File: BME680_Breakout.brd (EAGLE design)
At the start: 160 x 100 mm, 14 parts, among them U1 BME680, U4 PCA9515ADP

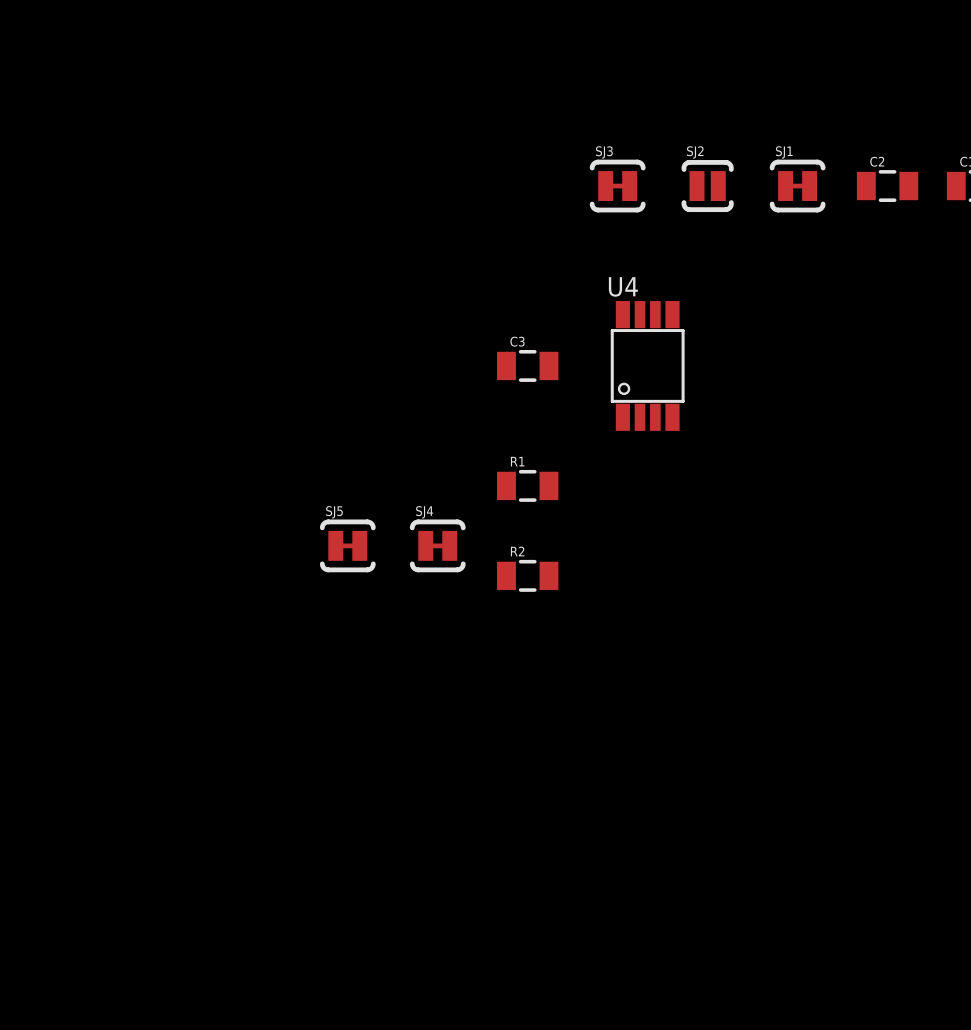
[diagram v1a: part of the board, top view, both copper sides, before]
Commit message: added some support for SPI and wired an 8-pin interface header
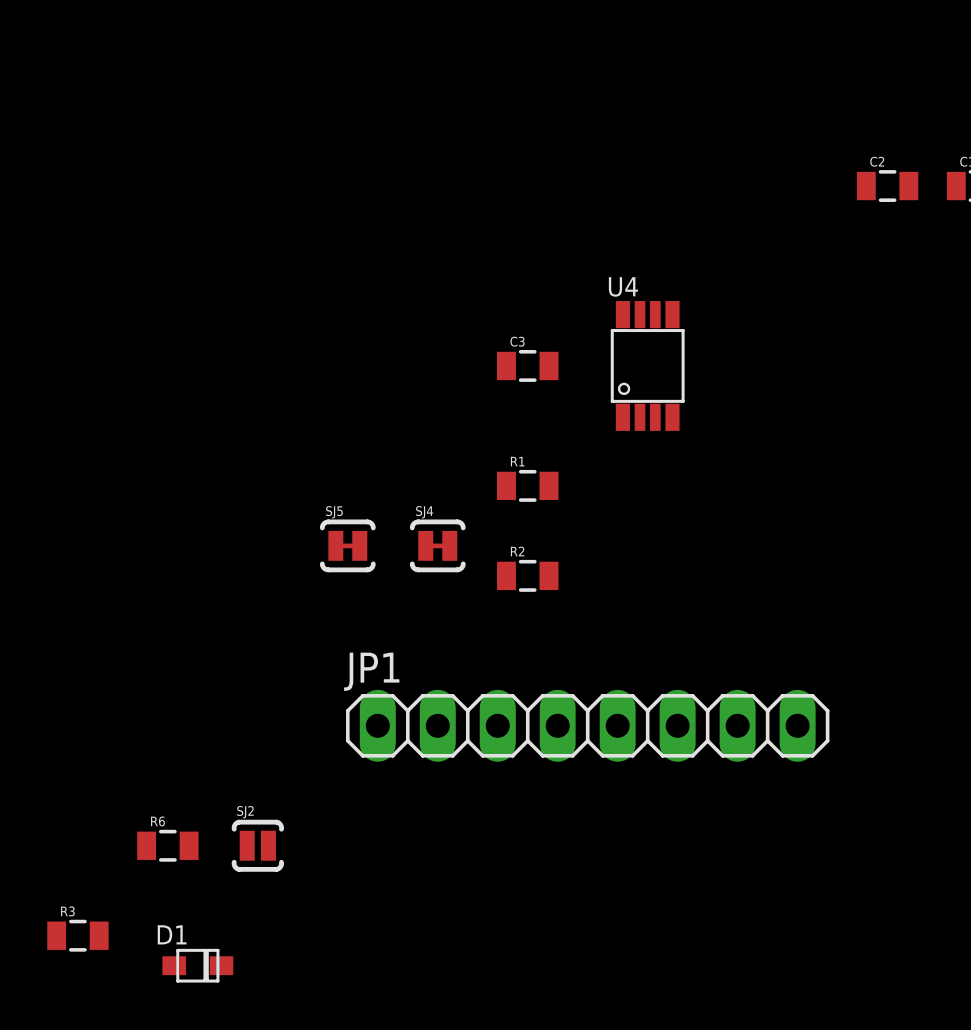
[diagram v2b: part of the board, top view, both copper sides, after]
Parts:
- removed SJ1, SJ3: JUMPER-PAD-2-NC_BY_TRACE, SparkFun-Passives:PAD-JUMPER-2-NC_BY_TRACE_YES_SILK
- added D1: (no value), adafruit:SOD-323F
- added JP1: (no value), pinhead:1X08
- added R3, R6: 10k, SparkFun-Passives:0805
- moved SJ2 33.8 mm to (-49.5, -25.4)
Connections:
- new net CSB_VCCIO: D1.C, JP1.6
- net 3.3V: now also JP1.8, R3.1, R6.1; no longer SJ2.2, SJ3.2
- net ADDR_SELECT_3V3: now also JP1.7, R3.2, SJ2.2; no longer SJ1.2, SJ2.1
- net CSB_3V3: now also D1.A, R6.2; no longer SJ3.1
- net GND: now also JP1.2, SJ2.1; no longer SJ1.1
- net MASTER_SCL_VIO: now also JP1.3
- net MASTER_SDA_VIO: now also JP1.4
- net SLAVE_I2C_ENABLE: now also JP1.5
- net VCCIO: now also JP1.1
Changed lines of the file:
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@@
 <element name="R5" library="SparkFun-Passives" package="0805" value="4.7k" x="-19.05" y="11.43"/>
 <element name="U1" library="wicked-device" package="BME680" value="BME680" x="-15.24" y="3.81"/>
-<element name="SJ1" library="SparkFun-Passives" package="PAD-JUMPER-2-NC_BY_TRACE_YES_SILK" value="JUMPER-PAD-2-NC_BY_TRACE" x="-26.67" y="2.54"/>
-<element name="SJ2" library="SparkFun-Passives" package="PAD-JUMPER-2-NO_YES_SILK" value="JUMPER-PAD-2-NOYES_SILK" x="-30.48" y="2.54"/>
-<element name="SJ3" library="SparkFun-Passives" package="PAD-JUMPER-2-NC_BY_TRACE_YES_SILK" value="JUMPER-PAD-2-NC_BY_TRACE" x="-34.29" y="2.54"/>
 <element name="U4" library="PCA9515ADP" package="SOT505-1" value="PCA9515ADP" x="-33.02" y="-5.08"/>
 <element name="C3" library="SparkFun-Passives" package="0805" value="0.1uF" x="-38.1" y="-5.08"/>
@@
 <element name="SJ4" library="SparkFun-Passives" package="PAD-JUMPER-2-NC_BY_TRACE_YES_SILK" value="JUMPER-PAD-2-NC_BY_TRACE" x="-41.91" y="-12.7"/>
 <element name="SJ5" library="SparkFun-Passives" package="PAD-JUMPER-2-NC_BY_TRACE_YES_SILK" value="JUMPER-PAD-2-NC_BY_TRACE" x="-45.72" y="-12.7"/>
+<element name="JP1" library="pinhead" package="1X08" value="" x="-35.56" y="-20.32"/>
+<element name="SJ2" library="SparkFun-Passives" package="PAD-JUMPER-2-NO_YES_SILK" value="JUMPER-PAD-2-NOYES_SILK" x="-49.53" y="-25.4"/>
+<element name="R6" library="SparkFun-Passives" package="0805" value="10k" x="-53.34" y="-25.4"/>
+<element name="D1" library="adafruit" package="SOD-323F" value="" x="-52.07" y="-30.48"/>
+<element name="R3" library="SparkFun-Passives" package="0805" value="10k" x="-57.15" y="-29.21"/>
 </elements>
 <signals>
@@
 <contactref element="R4" pad="1"/>
 <contactref element="R5" pad="1"/>
-<contactref element="SJ2" pad="2"/>
-<contactref element="SJ3" pad="2"/>
 <contactref element="U4" pad="8"/>
 <contactref element="C3" pad="1"/>
+<contactref element="R6" pad="1"/>
+<contactref element="R3" pad="1"/>
+<contactref element="JP1" pad="8"/>
+<wire x1="-54.24" y1="-25.4" x2="-58.05" y2="-29.21" width="0" layer="19" extent="1-1"/>
+<wire x1="-39" y1="-5.08" x2="-54.24" y2="-25.4" width="0" layer="19" extent="1-1"/>
 <wire x1="-34.07" y1="-2.905" x2="-39" y2="-5.08" width="0" layer="19" extent="1-1"/>
-<wire x1="-33.782" y1="2.54" x2="-34.07" y2="-2.905" width="0" layer="19" extent="1-1"/>
-<wire x1="-30.03" y1="2.54" x2="-33.782" y2="2.54" width="0" layer="19" extent="1-1"/>
-<wire x1="-23.76" y1="2.54" x2="-30.03" y2="2.54" width="0" layer="19" extent="1-1"/>
+<wire x1="-23.76" y1="2.54" x2="-34.07" y2="-2.905" width="0" layer="19" extent="1-1"/>
 <wire x1="-19.95" y1="2.54" x2="-23.76" y2="2.54" width="0" layer="19" extent="1-1"/>
 <wire x1="-16.5275" y1="3.41" x2="-19.95" y2="2.54" width="0" layer="19" extent="1-1"/>
@@
 <wire x1="-16.14" y1="11.43" x2="-16.5275" y2="5.01" width="0" layer="19" extent="1-1"/>
 <wire x1="-19.95" y1="11.43" x2="-16.14" y2="11.43" width="0" layer="19" extent="1-1"/>
+<wire x1="-26.67" y1="-20.32" x2="-34.07" y2="-2.905" width="0" layer="19" extent="1-1"/>
 </signal>
 <signal name="GND">
@@
 <contactref element="U1" pad="1"/>
 <contactref element="U1" pad="7"/>
-<contactref element="SJ1" pad="1"/>
 <contactref element="U4" pad="4"/>
 <contactref element="C3" pad="2"/>
+<contactref element="SJ2" pad="1"/>
+<contactref element="JP1" pad="2"/>
+<wire x1="-41.91" y1="-20.32" x2="-49.98" y2="-25.4" width="0" layer="19" extent="1-1"/>
+<wire x1="-37.2" y1="-5.08" x2="-41.91" y2="-20.32" width="0" layer="19" extent="1-1"/>
 <wire x1="-31.97" y1="-7.255" x2="-37.2" y2="-5.08" width="0" layer="19" extent="1-1"/>
-<wire x1="-27.178" y1="2.54" x2="-31.97" y2="-7.255" width="0" layer="19" extent="1-1"/>
-<wire x1="-21.96" y1="2.54" x2="-27.178" y2="2.54" width="0" layer="19" extent="1-1"/>
+<wire x1="-21.96" y1="2.54" x2="-31.97" y2="-7.255" width="0" layer="19" extent="1-1"/>
 <wire x1="-18.15" y1="2.54" x2="-21.96" y2="2.54" width="0" layer="19" extent="1-1"/>
 <wire x1="-16.5275" y1="4.21" x2="-18.15" y2="2.54" width="0" layer="19" extent="1-1"/>
@@
 <signal name="CSB_3V3">
 <contactref element="U1" pad="2"/>
-<contactref element="SJ3" pad="1"/>
-<wire x1="-13.9525" y1="4.21" x2="-34.798" y2="2.54" width="0" layer="19" extent="1-1"/>
+<contactref element="R6" pad="2"/>
+<contactref element="D1" pad="A"/>
+<wire x1="-52.44" y1="-25.4" x2="-53.07" y2="-30.48" width="0" layer="19" extent="1-1"/>
+<wire x1="-13.9525" y1="4.21" x2="-52.44" y2="-25.4" width="0" layer="19" extent="1-1"/>
 </signal>
 <signal name="ADDR_SELECT_3V3">
 <contactref element="U1" pad="5"/>
-<contactref element="SJ2" pad="1"/>
-<contactref element="SJ1" pad="2"/>
-<wire x1="-26.162" y1="2.54" x2="-30.93" y2="2.54" width="0" layer="19" extent="1-1"/>
-<wire x1="-16.5275" y1="2.61" x2="-26.162" y2="2.54" width="0" layer="19" extent="1-1"/>
+<contactref element="SJ2" pad="2"/>
+<contactref element="R3" pad="2"/>
+<contactref element="JP1" pad="7"/>
+<wire x1="-49.08" y1="-25.4" x2="-56.25" y2="-29.21" width="0" layer="19" extent="1-1"/>
+<wire x1="-29.21" y1="-20.32" x2="-49.08" y2="-25.4" width="0" layer="19" extent="1-1"/>
+<wire x1="-16.5275" y1="2.61" x2="-29.21" y2="-20.32" width="0" layer="19" extent="1-1"/>
 </signal>
 <signal name="SLAVE_SCL_3V3">
@@
 <signal name="MASTER_SCL_VIO">
 <contactref element="U4" pad="2"/>
+<contactref element="JP1" pad="3"/>
+<wire x1="-33.345" y1="-7.255" x2="-39.37" y2="-20.32" width="0" layer="19" extent="1-1"/>
 </signal>
 <signal name="MASTER_SDA_VIO">
 <contactref element="U4" pad="3"/>
+<contactref element="JP1" pad="4"/>
+<wire x1="-32.695" y1="-7.255" x2="-36.83" y2="-20.32" width="0" layer="19" extent="1-1"/>
 </signal>
 <signal name="SLAVE_I2C_ENABLE">
 <contactref element="U4" pad="5"/>
+<contactref element="JP1" pad="5"/>
+<wire x1="-31.97" y1="-2.905" x2="-34.29" y2="-20.32" width="0" layer="19" extent="1-1"/>
 </signal>
 <signal name="SLAVE_SDA_3V3">
@@
 <contactref element="R1" pad="1"/>
 <contactref element="R2" pad="1"/>
+<contactref element="JP1" pad="1"/>
+<wire x1="-39" y1="-13.97" x2="-44.45" y2="-20.32" width="0" layer="19" extent="1-1"/>
 <wire x1="-39" y1="-10.16" x2="-39" y2="-13.97" width="0" layer="19" extent="1-1"/>
 </signal>
@@
 <contactref element="SJ5" pad="1"/>
 </signal>
+<signal name="CSB_VCCIO">
+<contactref element="D1" pad="C"/>
+<contactref element="JP1" pad="6"/>
+<wire x1="-31.75" y1="-20.32" x2="-51.07" y2="-30.48" width="0" layer="19" extent="1-1"/>
+</signal>
 </signals>

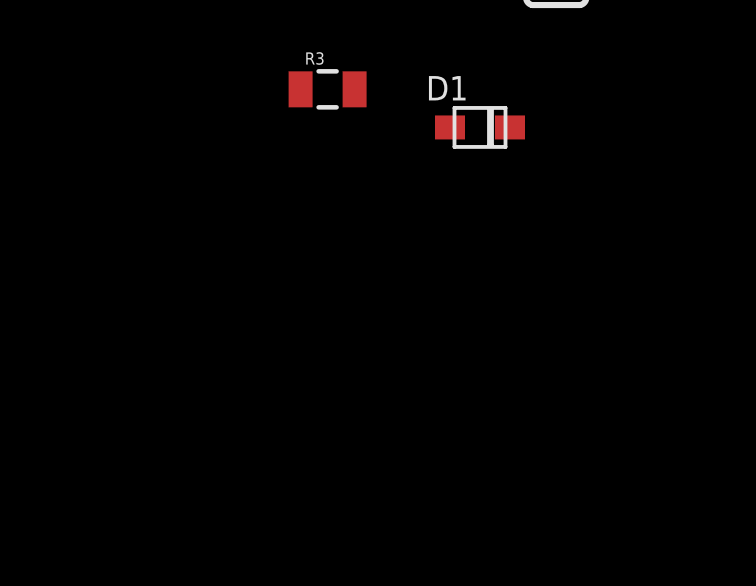
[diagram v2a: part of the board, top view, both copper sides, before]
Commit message: added input power regulator, still need bypass solution, reorganized schematic slightly
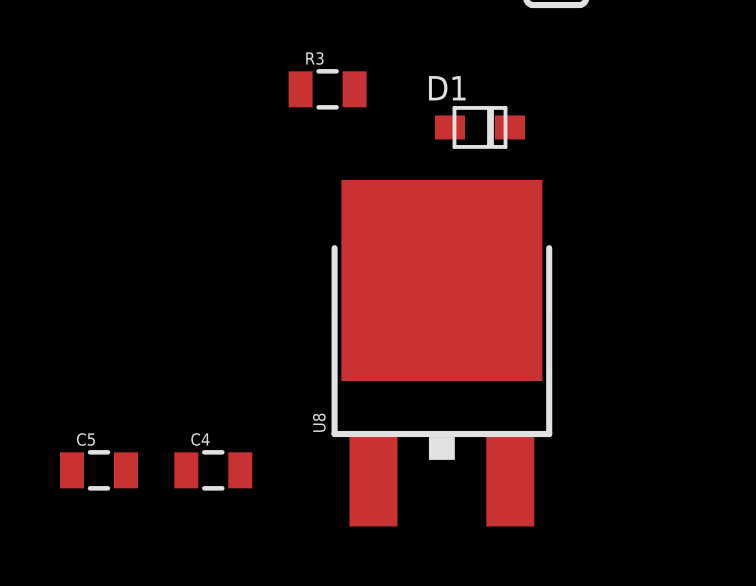
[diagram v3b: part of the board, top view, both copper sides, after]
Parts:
- added C4, C5: 10uF, SparkFun-Passives:0805
- added U8: LD1117XX, wicked-device:DPAK
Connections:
- net 3.3V: now also C5.1, U8.4
- net GND: now also C4.2, C5.2, U8.1
- net VCCIO: now also C4.1, U8.3
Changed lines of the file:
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@@
 <layer number="113" name="IDFDebug" color="4" fill="1" visible="yes" active="yes"/>
 <layer number="116" name="Patch_BOT" color="9" fill="4" visible="yes" active="yes"/>
+<layer number="118" name="Rect_Pads" color="7" fill="1" visible="no" active="yes"/>
 <layer number="121" name="_tsilk" color="7" fill="1" visible="yes" active="yes"/>
 <layer number="122" name="_bsilk" color="7" fill="1" visible="yes" active="yes"/>
@@
 <layer number="223" name="223bmp" color="24" fill="1" visible="no" active="no"/>
 <layer number="224" name="224bmp" color="25" fill="1" visible="no" active="no"/>
+<layer number="231" name="Eagle3D_PG1" color="7" fill="1" visible="yes" active="yes"/>
+<layer number="232" name="Eagle3D_PG2" color="7" fill="1" visible="yes" active="yes"/>
+<layer number="233" name="Eagle3D_PG3" color="7" fill="1" visible="yes" active="yes"/>
 <layer number="248" name="Housing" color="7" fill="1" visible="yes" active="yes"/>
 <layer number="249" name="Edge" color="7" fill="1" visible="yes" active="yes"/>
@@
 <element name="D1" library="adafruit" package="SOD-323F" value="" x="-52.07" y="-30.48"/>
 <element name="R3" library="SparkFun-Passives" package="0805" value="10k" x="-57.15" y="-29.21"/>
+<element name="U8" library="wicked-device" package="DPAK" value="LD1117XX" x="-53.34" y="-39.37"/>
+<element name="C4" library="SparkFun-Passives" package="0805" value="10uF" x="-60.96" y="-41.91"/>
+<element name="C5" library="SparkFun-Passives" package="0805" value="10uF" x="-64.77" y="-41.91"/>
 </elements>
 <signals>
@@
 <contactref element="R3" pad="1"/>
 <contactref element="JP1" pad="8"/>
+<contactref element="U8" pad="4"/>
+<contactref element="C5" pad="1"/>
+<wire x1="-53.34" y1="-35.582" x2="-65.67" y2="-41.91" width="0" layer="19" extent="1-1"/>
+<wire x1="-58.05" y1="-29.21" x2="-53.34" y2="-35.582" width="0" layer="19" extent="1-1"/>
 <wire x1="-54.24" y1="-25.4" x2="-58.05" y2="-29.21" width="0" layer="19" extent="1-1"/>
 <wire x1="-39" y1="-5.08" x2="-54.24" y2="-25.4" width="0" layer="19" extent="1-1"/>
@@
 <contactref element="SJ2" pad="1"/>
 <contactref element="JP1" pad="2"/>
+<contactref element="U8" pad="1"/>
+<contactref element="C4" pad="2"/>
+<contactref element="C5" pad="2"/>
+<wire x1="-60.06" y1="-41.91" x2="-63.87" y2="-41.91" width="0" layer="19" extent="1-1"/>
+<wire x1="-55.62" y1="-42.28" x2="-60.06" y2="-41.91" width="0" layer="19" extent="1-1"/>
+<wire x1="-49.98" y1="-25.4" x2="-55.62" y2="-42.28" width="0" layer="19" extent="1-1"/>
 <wire x1="-41.91" y1="-20.32" x2="-49.98" y2="-25.4" width="0" layer="19" extent="1-1"/>
 <wire x1="-37.2" y1="-5.08" x2="-41.91" y2="-20.32" width="0" layer="19" extent="1-1"/>
@@
 <contactref element="R2" pad="1"/>
 <contactref element="JP1" pad="1"/>
+<contactref element="U8" pad="3"/>
+<contactref element="C4" pad="1"/>
+<wire x1="-51.06" y1="-42.28" x2="-61.86" y2="-41.91" width="0" layer="19" extent="1-1"/>
+<wire x1="-44.45" y1="-20.32" x2="-51.06" y2="-42.28" width="0" layer="19" extent="1-1"/>
 <wire x1="-39" y1="-13.97" x2="-44.45" y2="-20.32" width="0" layer="19" extent="1-1"/>
 <wire x1="-39" y1="-10.16" x2="-39" y2="-13.97" width="0" layer="19" extent="1-1"/>

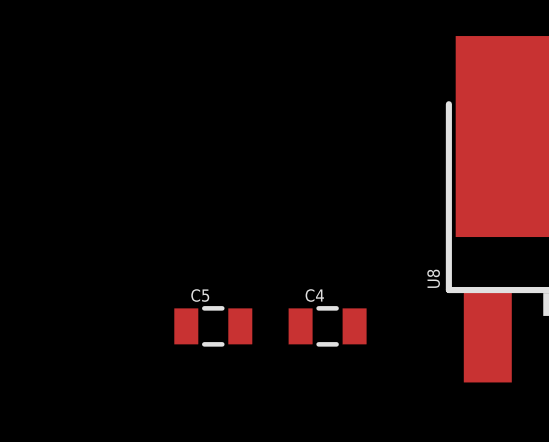
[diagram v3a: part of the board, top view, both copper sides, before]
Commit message: added pull-down hardware option to allow changing default behavior of i2c buffer
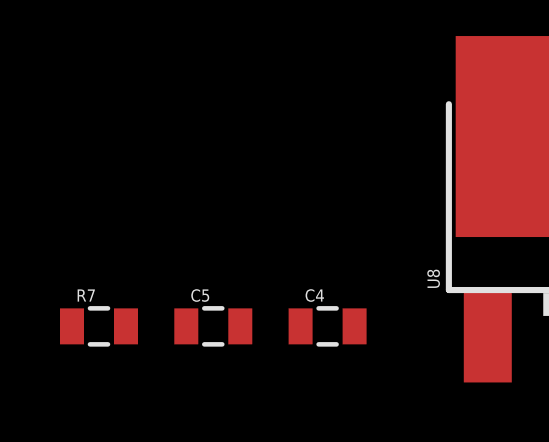
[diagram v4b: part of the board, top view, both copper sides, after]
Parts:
- added R7: 10k_DNP, SparkFun-Passives:0805
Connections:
- net CSB_VCCIO renamed CSB_VIO
- net GND: now also R7.2
- net SLAVE_I2C_ENABLE: now also R7.1
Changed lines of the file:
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@@
 <element name="C4" library="SparkFun-Passives" package="0805" value="10uF" x="-60.96" y="-41.91"/>
 <element name="C5" library="SparkFun-Passives" package="0805" value="10uF" x="-64.77" y="-41.91"/>
+<element name="R7" library="SparkFun-Passives" package="0805" value="10k_DNP" x="-68.58" y="-41.91"/>
 </elements>
 <signals>
@@
 <contactref element="C4" pad="2"/>
 <contactref element="C5" pad="2"/>
+<contactref element="R7" pad="2"/>
+<wire x1="-63.87" y1="-41.91" x2="-67.68" y2="-41.91" width="0" layer="19" extent="1-1"/>
 <wire x1="-60.06" y1="-41.91" x2="-63.87" y2="-41.91" width="0" layer="19" extent="1-1"/>
 <wire x1="-55.62" y1="-42.28" x2="-60.06" y2="-41.91" width="0" layer="19" extent="1-1"/>
@@
 <contactref element="U4" pad="5"/>
 <contactref element="JP1" pad="5"/>
+<contactref element="R7" pad="1"/>
+<wire x1="-34.29" y1="-20.32" x2="-69.48" y2="-41.91" width="0" layer="19" extent="1-1"/>
 <wire x1="-31.97" y1="-2.905" x2="-34.29" y2="-20.32" width="0" layer="19" extent="1-1"/>
 </signal>
@@
 <contactref element="SJ5" pad="1"/>
 </signal>
-<signal name="CSB_VCCIO">
+<signal name="CSB_VIO">
 <contactref element="D1" pad="C"/>
 <contactref element="JP1" pad="6"/>

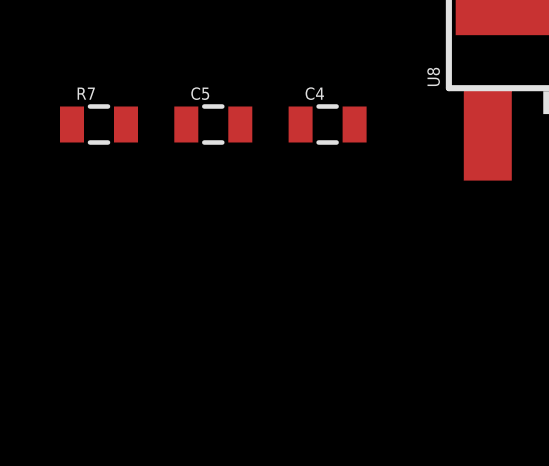
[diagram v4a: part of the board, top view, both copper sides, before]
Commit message: added a few internal test points
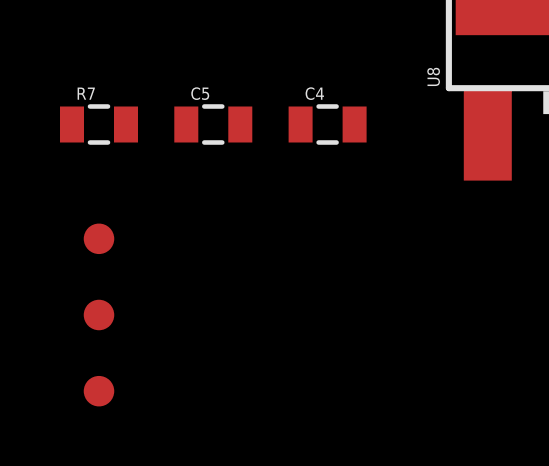
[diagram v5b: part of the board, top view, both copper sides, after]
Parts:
- added TP1, TP2, TP3: TEST-POINT3X4, SparkFun-Passives:PAD.03X.04
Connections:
- removed net N$1: R1.2, SJ4.2
- removed net N$2: R2.2, SJ5.2
- new net SJ_MASTER_SCL_3V3: R2.2, SJ5.2, TP2.P$1
- new net SJ_MASTER_SDA_3V3: R1.2, SJ4.2, TP1.P$1
- net CSB_3V3: now also TP3.P$1
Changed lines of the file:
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@@
 <element name="C5" library="SparkFun-Passives" package="0805" value="10uF" x="-64.77" y="-41.91"/>
 <element name="R7" library="SparkFun-Passives" package="0805" value="10k_DNP" x="-68.58" y="-41.91"/>
+<element name="TP1" library="SparkFun-Passives" package="PAD.03X.04" value="TEST-POINT3X4" x="-68.58" y="-45.72"/>
+<element name="TP2" library="SparkFun-Passives" package="PAD.03X.04" value="TEST-POINT3X4" x="-68.58" y="-48.26"/>
+<element name="TP3" library="SparkFun-Passives" package="PAD.03X.04" value="TEST-POINT3X4" x="-68.58" y="-50.8"/>
 </elements>
 <signals>
@@
 <contactref element="R6" pad="2"/>
 <contactref element="D1" pad="A"/>
+<contactref element="TP3" pad="P$1"/>
+<wire x1="-53.07" y1="-30.48" x2="-68.58" y2="-50.8" width="0" layer="19" extent="1-1"/>
 <wire x1="-52.44" y1="-25.4" x2="-53.07" y2="-30.48" width="0" layer="19" extent="1-1"/>
 <wire x1="-13.9525" y1="4.21" x2="-52.44" y2="-25.4" width="0" layer="19" extent="1-1"/>
@@
 <wire x1="-39" y1="-10.16" x2="-39" y2="-13.97" width="0" layer="19" extent="1-1"/>
 </signal>
-<signal name="N$1">
+<signal name="SJ_MASTER_SDA_3V3">
 <contactref element="R1" pad="2"/>
 <contactref element="SJ4" pad="2"/>
+<contactref element="TP1" pad="P$1"/>
+<wire x1="-41.402" y1="-12.7" x2="-68.58" y2="-45.72" width="0" layer="19" extent="1-1"/>
 <wire x1="-37.2" y1="-10.16" x2="-41.402" y2="-12.7" width="0" layer="19" extent="1-1"/>
 </signal>
-<signal name="N$2">
+<signal name="SJ_MASTER_SCL_3V3">
 <contactref element="R2" pad="2"/>
 <contactref element="SJ5" pad="2"/>
+<contactref element="TP2" pad="P$1"/>
+<wire x1="-45.212" y1="-12.7" x2="-68.58" y2="-48.26" width="0" layer="19" extent="1-1"/>
 <wire x1="-37.2" y1="-13.97" x2="-45.212" y2="-12.7" width="0" layer="19" extent="1-1"/>
 </signal>
